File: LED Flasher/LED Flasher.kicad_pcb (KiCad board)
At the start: 2 copper layers, 37.4 x 37.4 mm, 20 parts, among them Q1 BC848, Q2 BC848, Q3 BC858, Q4 SI2342DS-T1-GE3

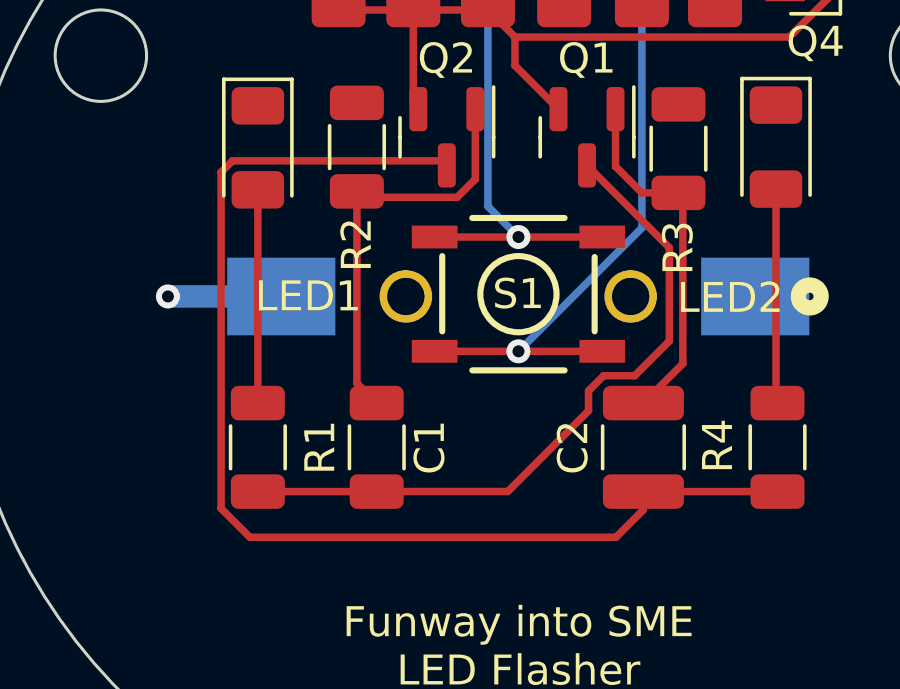
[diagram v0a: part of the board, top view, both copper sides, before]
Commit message: Updates and improvements to LED Flasher
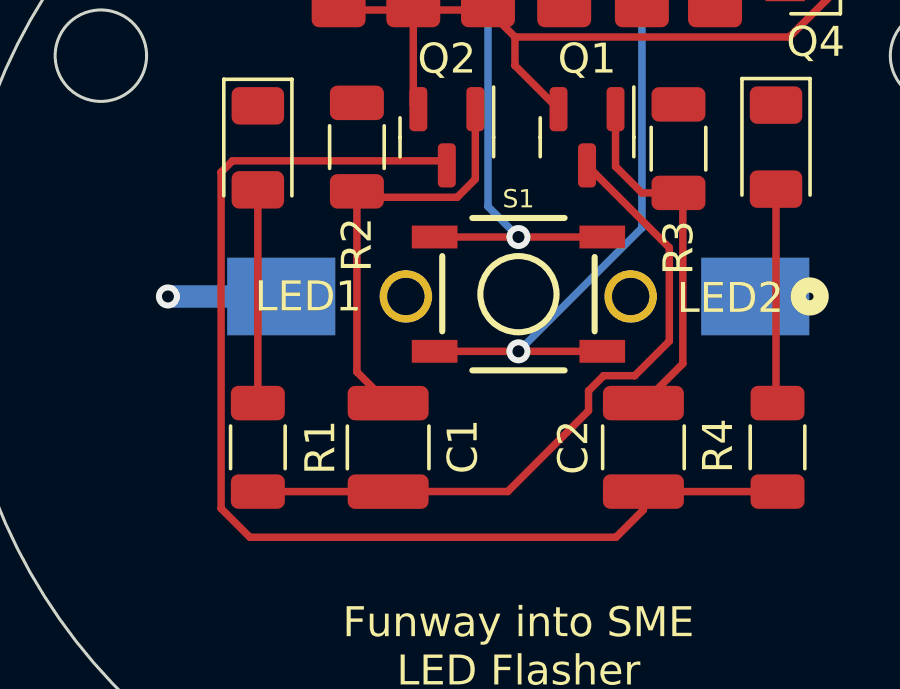
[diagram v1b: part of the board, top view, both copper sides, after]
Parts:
- C1: value 2.2UF-1206-50V-10% -> 100UF-1210-50V-20%; footprint Capacitor_SMD:C_1206_3216Metric -> Capacitor_SMD:C_1210_3225Metric
- C2: value 10UF-1210-50V-20% -> 100UF-1210-50V-20%
- Q4: value SI2342DS-T1-GE3 -> SI2338DS
- R1, R4: value 15R -> 51R
- moved C1 0.38 mm to (154.8, 99.5)
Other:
- board text added: "+IVE"
- board text added: "GND"
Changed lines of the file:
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@@
   (net 12 "Net-(Q3-C)")
   (net 13 "Net-(Q4-Pad1)")
+  (footprint "Capacitor_SMD:C_1210_3225Metric" (layer "F.Cu")
+    (at 154.813 99.519 90)
+    (descr "Capacitor SMD 1210 (3225 Metric), square (rectangular) end terminal, IPC_7351 nominal, (Body size source: IPC-SM-782 page 76, https://www.pcb-3d.com/wordpress/wp-content/uploads/ipc-sm-782a_amendment_1_and_2.pdf), generated with kicad-footprint-generator")
+    (tags "capacitor")
+    (property "Field4" "CAP-09824")
+    (property "Sheetfile" "LED Flasher.kicad_sch")
+    (property "Sheetname" "")
+    (property "ki_description" "10.0uF ceramic capacitors A capacitor is a passive two-terminal electrical component used to store electrical energy temporarily in an electric field.")
+    (property "ki_keywords" "PROD_ID:CAP-09824")
+    (attr smd)
+    (fp_text reference "C1" (at 0.0272 2.4892 90) (layer "F.SilkS")
+        (effects (font (size 1 1) (thickness 0.15)))
+    )
+    (fp_text value "100UF-1210-50V-20%" (at 0 2.3 90) (layer "F.Fab")
+        (effects (font (size 1 1) (thickness 0.15)))
+    )
+    (fp_text user "${REFERENCE}" (at 0 0 90) (layer "F.Fab")
+        (effects (font (size 0.8 0.8) (thickness 0.12)))
+    )
+    (fp_line (start -0.711252 -1.36) (end 0.711252 -1.36)
+      (stroke (width 0.12) (type solid)) (layer "F.SilkS"))
+    (fp_line (start -0.711252 1.36) (end 0.711252 1.36)
+      (stroke (width 0.12) (type solid)) (layer "F.SilkS"))
+    (fp_line (start -2.3 -1.6) (end 2.3 -1.6)
+      (stroke (width 0.05) (type solid)) (layer "F.CrtYd"))
+    (fp_line (start -2.3 1.6) (end -2.3 -1.6)
+      (stroke (width 0.05) (type solid)) (layer "F.CrtYd"))
+    (fp_line (start 2.3 -1.6) (end 2.3 1.6)
+      (stroke (width 0.05) (type solid)) (layer "F.CrtYd"))
+    (fp_line (start 2.3 1.6) (end -2.3 1.6)
+      (stroke (width 0.05) (type solid)) (layer "F.CrtYd"))
+    (fp_line (start -1.6 -1.25) (end 1.6 -1.25)
+      (stroke (width 0.1) (type solid)) (layer "F.Fab"))
+    (fp_line (start -1.6 1.25) (end -1.6 -1.25)
+      (stroke (width 0.1) (type solid)) (layer "F.Fab"))
+    (fp_line (start 1.6 -1.25) (end 1.6 1.25)
+      (stroke (width 0.1) (type solid)) (layer "F.Fab"))
+    (fp_line (start 1.6 1.25) (end -1.6 1.25)
+      (stroke (width 0.1) (type solid)) (layer "F.Fab"))
+    (pad "1" smd roundrect (at -1.475 0 90) (size 1.15 2.7) (layers "F.Cu" "F.Paste" "F.Mask") (roundrect_rratio 0.217391)
+      (net 1 "Net-(Q1-C)") (pinfunction "1") (pintype "passive"))
+    (pad "2" smd roundrect (at 1.475 0 90) (size 1.15 2.7) (layers "F.Cu" "F.Paste" "F.Mask") (roundrect_rratio 0.217391)
+      (net 2 "LED 2") (pinfunction "2") (pintype "passive"))
+    (model "${KICAD6_3DMODEL_DIR}/Capacitor_SMD.3dshapes/C_1210_3225Metric.wrl"
+      (offset (xyz 0 0 0))
+      (scale (xyz 1 1 1))
+      (rotate (xyz 0 0 0))
+    )
+  )
   (footprint "Capacitor_SMD:C_1206_3216Metric" (layer "F.Cu")
     (at 153.162 83.4644 90)
@@
     (property "ki_keywords" "PROD_ID:SWCH-08247")
     (attr smd)
-    (fp_text reference "S1" (at 0 0) (layer "F.SilkS")
-        (effects (font (size 1 1) (thickness 0.127)))
+    (fp_text reference "S1" (at 0 -3.175) (layer "F.SilkS")
+        (effects (font (size 0.6096 0.6096) (thickness 0.127)))
     )
     (fp_text value "MOMENTARY-SWITCH-SPST-2-SMD-5.2MM" (at 0 3.175) (layer "F.SilkS") hide
@@
         (effects (font (size 1 1) (thickness 0.15)))
     )
-    (fp_text value "15R" (at 0 1.85 90) (layer "F.Fab")
+    (fp_text value "51R" (at 0 1.85 90) (layer "F.Fab")
         (effects (font (size 1 1) (thickness 0.15)))
     )
@@
         (effects (font (size 1 1) (thickness 0.15)))
     )
-    (fp_text value "10UF-1210-50V-20%" (at 0 2.3 90) (layer "F.Fab")
+    (fp_text value "100UF-1210-50V-20%" (at 0 2.3 90) (layer "F.Fab")
         (effects (font (size 1 1) (thickness 0.15)))
     )
@@
         (effects (font (size 1 1) (thickness 0.15)))
     )
-    (fp_text value "15R" (at 0 1.85 90) (layer "F.Fab")
+    (fp_text value "51R" (at 0 1.85 90) (layer "F.Fab")
         (effects (font (size 1 1) (thickness 0.15)))
     )
@@
   )
   (footprint "Capacitor_SMD:C_1206_3216Metric" (layer "F.Cu")
-    (at 154.432 99.5172 90)
-    (descr "Capacitor SMD 1206 (3216 Metric), square (rectangular) end terminal, IPC_7351 nominal, (Body size source: IPC-SM-782 page 76, https://www.pcb-3d.com/wordpress/wp-content/uploads/ipc-sm-782a_amendment_1_and_2.pdf), generated with kicad-footprint-generator")
-    (tags "capacitor")
-    (property "Field4" "CAP-10009")
-    (property "Sheetfile" "LED Flasher.kicad_sch")
-    (property "Sheetname" "")
-    (property "ki_description" "2.2uF ceramic capacitors A capacitor is a passive two-terminal electrical component used to store electrical energy temporarily in an electric field.")
-    (property "ki_keywords" "PROD_ID:CAP-10009")
-    (attr smd)
-    (fp_text reference "C1" (at 0 1.778 90) (layer "F.SilkS")
-        (effects (font (size 1 1) (thickness 0.15)))
-    )
-    (fp_text value "2.2UF-1206-50V-10%" (at 0 1.85 90) (layer "F.Fab")
-        (effects (font (size 1 1) (thickness 0.15)))
-    )
-    (fp_text user "${REFERENCE}" (at 0 0 90) (layer "F.Fab")
-        (effects (font (size 0.8 0.8) (thickness 0.12)))
-    )
-    (fp_line (start -0.711252 -0.91) (end 0.711252 -0.91)
-      (stroke (width 0.12) (type solid)) (layer "F.SilkS"))
-    (fp_line (start -0.711252 0.91) (end 0.711252 0.91)
-      (stroke (width 0.12) (type solid)) (layer "F.SilkS"))
-    (fp_line (start -2.3 -1.15) (end 2.3 -1.15)
-      (stroke (width 0.05) (type solid)) (layer "F.CrtYd"))
-    (fp_line (start -2.3 1.15) (end -2.3 -1.15)
-      (stroke (width 0.05) (type solid)) (layer "F.CrtYd"))
-    (fp_line (start 2.3 -1.15) (end 2.3 1.15)
-      (stroke (width 0.05) (type solid)) (layer "F.CrtYd"))
-    (fp_line (start 2.3 1.15) (end -2.3 1.15)
-      (stroke (width 0.05) (type solid)) (layer "F.CrtYd"))
-    (fp_line (start -1.6 -0.8) (end 1.6 -0.8)
-      (stroke (width 0.1) (type solid)) (layer "F.Fab"))
-    (fp_line (start -1.6 0.8) (end -1.6 -0.8)
-      (stroke (width 0.1) (type solid)) (layer "F.Fab"))
-    (fp_line (start 1.6 -0.8) (end 1.6 0.8)
-      (stroke (width 0.1) (type solid)) (layer "F.Fab"))
-    (fp_line (start 1.6 0.8) (end -1.6 0.8)
-      (stroke (width 0.1) (type solid)) (layer "F.Fab"))
-    (pad "1" smd roundrect (at -1.475 0 90) (size 1.15 1.8) (layers "F.Cu" "F.Paste" "F.Mask") (roundrect_rratio 0.2173913043)
-      (net 1 "Net-(Q1-C)") (pinfunction "1") (pintype "passive"))
-    (pad "2" smd roundrect (at 1.475 0 90) (size 1.15 1.8) (layers "F.Cu" "F.Paste" "F.Mask") (roundrect_rratio 0.2173913043)
-      (net 2 "LED 2") (pinfunction "2") (pintype "passive"))
-    (model "${KICAD6_3DMODEL_DIR}/Capacitor_SMD.3dshapes/C_1206_3216Metric.wrl"
-      (offset (xyz 0 0 0))
-      (scale (xyz 1 1 1))
-      (rotate (xyz 0 0 0))
-    )
-  )
-  (footprint "Capacitor_SMD:C_1206_3216Metric" (layer "F.Cu")
     (at 155.6512 83.4644 90)
     (descr "Capacitor SMD 1206 (3216 Metric), square (rectangular) end terminal, IPC_7351 nominal, (Body size source: IPC-SM-782 page 76, https://www.pcb-3d.com/wordpress/wp-content/uploads/ipc-sm-782a_amendment_1_and_2.pdf), generated with kicad-footprint-generator")
@@
         (effects (font (size 1 1) (thickness 0.15)))
     )
-    (fp_text value "SI2342DS-T1-GE3" (at 0 0 90) (layer "F.SilkS") hide
+    (fp_text value "SI2338DS" (at 0 0 90) (layer "F.SilkS") hide
         (effects (font (size 1 1) (thickness 0.15)))
     )
@@
   (gr_circle (center 159.1564 94.488) (end 177.8508 94.5896)
     (stroke (width 0.1) (type default)) (fill none) (layer "Edge.Cuts"))
+  (gr_text "+IVE" (at 149.1742 94.996) (layer "B.SilkS")
+    (effects (font (size 1 1) (thickness 0.15)) (justify left bottom mirror))
+  )
+  (gr_text "GND" (at 172.593 95.123) (layer "B.SilkS")
+    (effects (font (size 1 1) (thickness 0.15)) (justify left bottom mirror))
+  )
   (gr_text "Funway into SME\nLED Flasher" (at 159.1564 107.5436) (layer "F.SilkS")
     (effects (font (size 1 1) (thickness 0.15)) (justify bottom))
@@
   (segment (start 164.1856 92.8624) (end 161.4424 90.1192) (width 0.25) (layer "F.Cu") (net 1))
   (segment (start 153.9687 91.1817) (end 153.7716 90.9846) (width 0.25) (layer "F.Cu") (net 2))
+  (segment (start 153.7716 97.0026) (end 154.813 98.044) (width 0.25) (layer "F.Cu") (net 2))
   (segment (start 157.115551 91.1817) (end 153.9687 91.1817) (width 0.25) (layer "F.Cu") (net 2))
   (segment (start 157.7188 90.578451) (end 157.115551 91.1817) (width 0.25) (layer "F.Cu") (net 2))
+  (segment (start 153.7716 90.9846) (end 153.7716 97.0026) (width 0.25) (layer "F.Cu") (net 2))
   (segment (start 157.7188 88.2442) (end 157.7188 90.578451) (width 0.25) (layer "F.Cu") (net 2))
-  (segment (start 153.7716 97.3818) (end 154.432 98.0422) (width 0.25) (layer "F.Cu") (net 2))
-  (segment (start 153.7716 90.9846) (end 153.7716 97.3818) (width 0.25) (layer "F.Cu") (net 2))
   (segment (start 163.273 91.0354) (end 164.4904 91.0354) (width 0.25) (layer "F.Cu") (net 3))
   (segment (start 164.6356 91.1806) (end 164.4904 91.0354) (width 0.25) (layer "F.Cu") (net 3))
